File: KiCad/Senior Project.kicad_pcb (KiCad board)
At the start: 4 copper layers, 25 x 60 mm, 90 parts, among them J1 USB_C_Receptacle_USB2.0_16P, J2 Screw_Terminal_01x02, J3 Screw_Terminal_01x06, J4 Conn_ARM_JTAG_SWD_10, J5 Conn_01x02, Q2 IRLML0030, Q3 IRLML0030, Q4 IRLML0030, SW1 SW_Push, SW2 SW_Push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

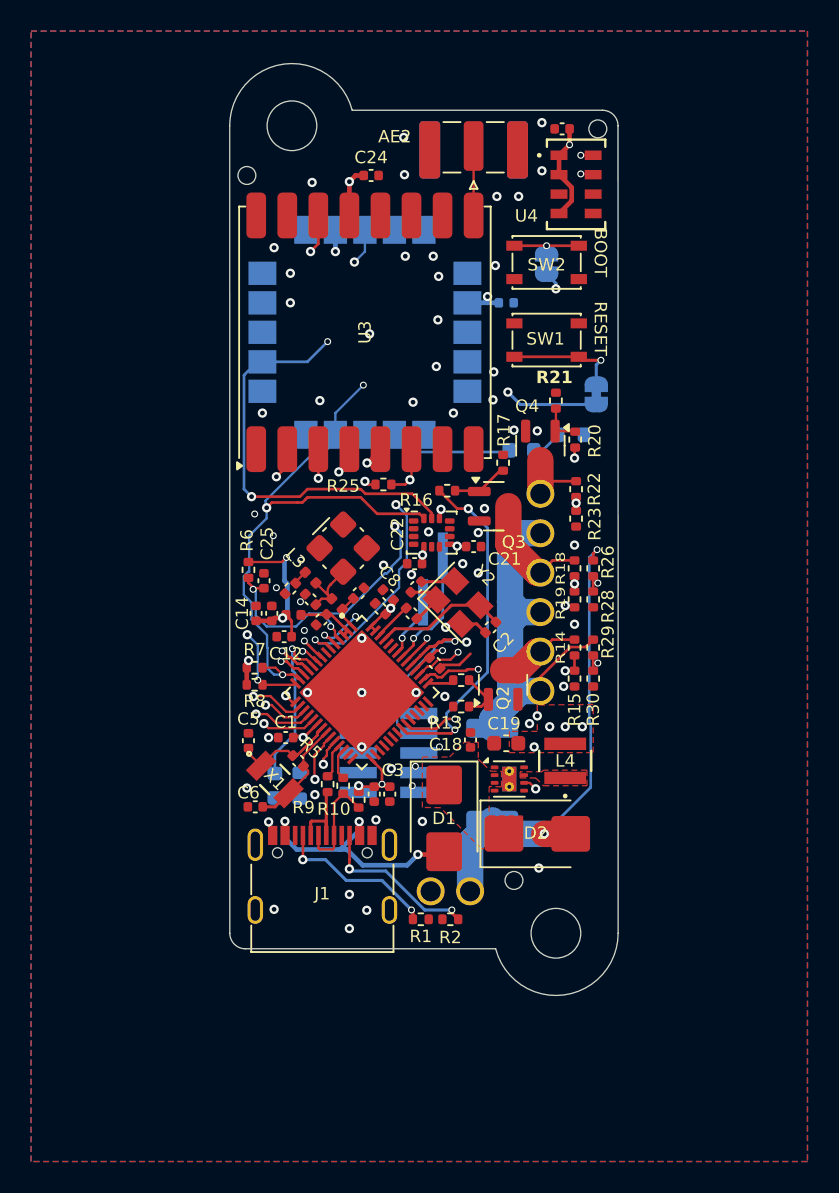
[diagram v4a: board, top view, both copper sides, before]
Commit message: switch to BMI088 for IMU
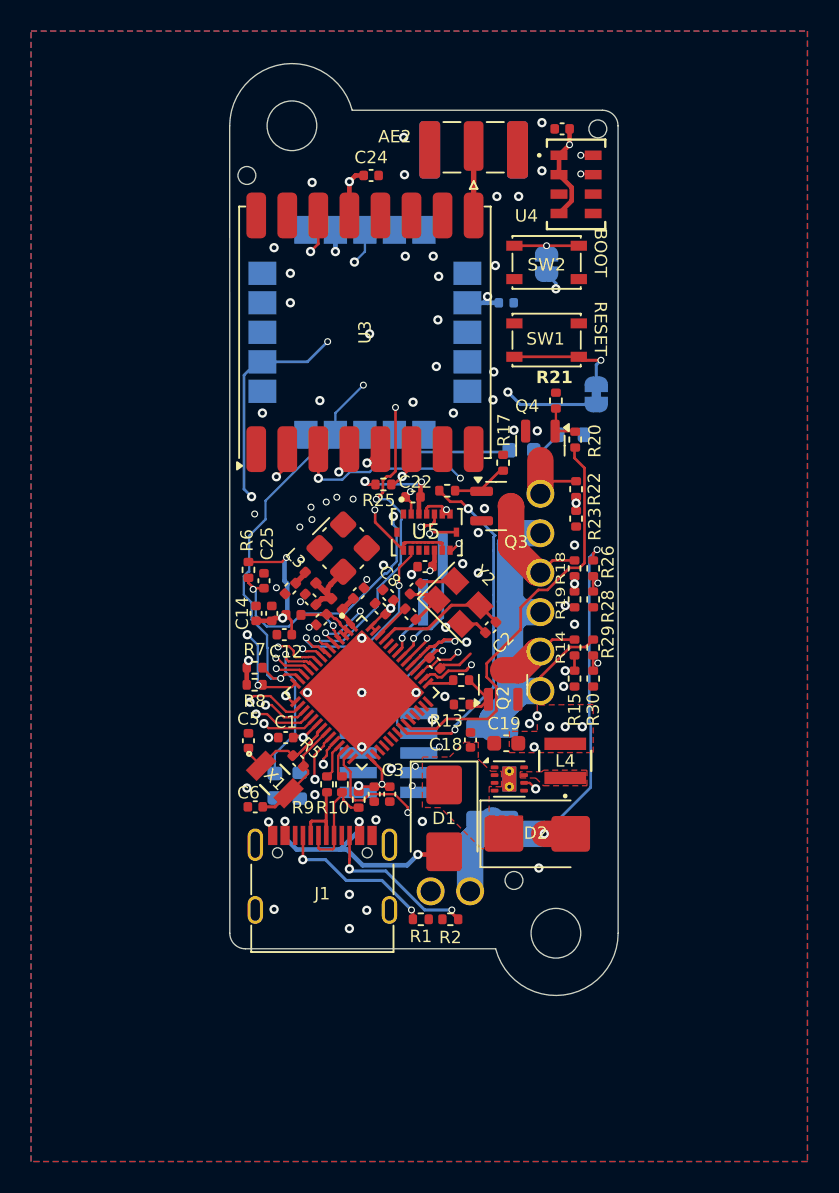
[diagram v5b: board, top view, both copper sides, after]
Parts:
- U5: value LSM6DSO32TR -> BMI088; footprint Package_LGA:LGA-14_3x2.5mm_P0.5mm_LayoutBorder3x4y -> asdt-4:PQFN50P450X300X100-16N
- moved C22 4.30 mm to (86.8, 84.9)
- moved C21 3.39 mm to (87.6, 89.4), turned to 180 degrees
- moved U5 0.32 mm to (87.7, 87.2)
- moved Q3 0.15 mm to (92.2, 85.5)
- moved R13 0.14 mm to (89.9, 98.3)
- moved C12 0.13 mm to (78.5, 93.8)
- moved C10 0.12 mm to (87.0, 90.8)
- moved R10 0.12 mm to (82.2, 103.4)
- moved R4 0.09 mm to (86.6, 92.5)
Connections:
- U1 pad 27: unconnected-(U1-GPIO21-Pad27) -> /~{GYRO_CS}
- U1 pad 7: unconnected-(U1-GPIO2-Pad7) -> /~{ACCELEROMETER_CS}
- U5 pad 1: GND -> unconnected-(U5-INT2-Pad1)
- U5 pad 10: unconnected-(U5-NC-Pad10) -> /FSPIQ
- U5 pad 11: unconnected-(U5-NC__1-Pad11) -> +3V3
- U5 pad 12: +3V3 -> unconnected-(U5-INT3-Pad12)
- U5 pad 13: /SCL -> unconnected-(U5-INT4-Pad13)
- U5 pad 14: /SDA -> /~{ACCELEROMETER_CS}
- U5 pad 3: GND -> +3V3
- U5 pad 4: unconnected-(U5-INT1-Pad4) -> GND
- U5 pad 5: +3V3 -> /~{GYRO_CS}
- U5 pad 8: +3V3 -> /FSPICLK
- U5 pad 9: unconnected-(U5-INT2-Pad9) -> /FSPID
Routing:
- net /~{GYRO_CS}: track 0.00 -> 47.1 mm, vias 0 -> 2
- net /FSPID: track 21.8 -> 41.1 mm, vias 2 -> 4
- net /FSPIQ: track 23.6 -> 41.8 mm, vias 2 -> 3
- net /~{ACCELEROMETER_CS}: track 0.00 -> 13.3 mm, vias 0 -> 2
- net /SCL: track 64.2 -> 51.7 mm
- net /SDA: track 58.0 -> 47.3 mm, vias 4 -> 3
- net /FSPICLK: track 22.3 -> 32.0 mm, vias 2 -> 3
- net /RADIO_RST: track 19.8 -> 23.9 mm
- net GND: track 6.37 -> 10.1 mm, vias 63 -> 70
- net /BATTERY_SENSE: track 26.6 -> 28.8 mm
- net /Pyro GPIO 3: track 25.8 -> 27.3 mm, vias 2 -> 0
- net +3V3: track 73.1 -> 71.7 mm, vias 21 -> 20
- net /FSPICS0: track 20.8 -> 21.9 mm
- net /GPS_Reset: track 31.1 -> 31.8 mm
- net /MTCK: track 13.8 -> 13.1 mm
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
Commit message: further refine board
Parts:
- R15, R19, R23: value 10k -> 5.1k
- moved J5 7.00 mm to (83.9, 95.8), turned to 180 degrees
- moved REF** 5.30 mm to (98.6, 109.7)
- moved C22 0.30 mm to (87.1, 84.9)
- moved Q2 0.22 mm to (92.5, 97.2)
- moved R13 0.19 mm to (89.8, 98.4)
- moved R11 0.19 mm to (91.9, 103.0)
- moved C5 0.15 mm to (76.2, 100.5)
- moved U4 0.12 mm to (97.3, 64.9)
- moved R12 0.07 mm to (89.8, 96.7)
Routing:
- net Net-(J5-Pin_1): track 7.93 -> 6.81 mm
- net /MTDI: track 12.7 -> 13.5 mm
- net +3V3: track 71.7 -> 72.3 mm
- net GND: track 10.1 -> 10.0 mm, vias 70 -> 82
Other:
- board text added: "+"
- board text added: "-"
- board text added: "A"
- board text added: "B"
- board text added: "C"
- board text added: "Max 4s"
- board text added: "PPS"
- board text added: "Status"

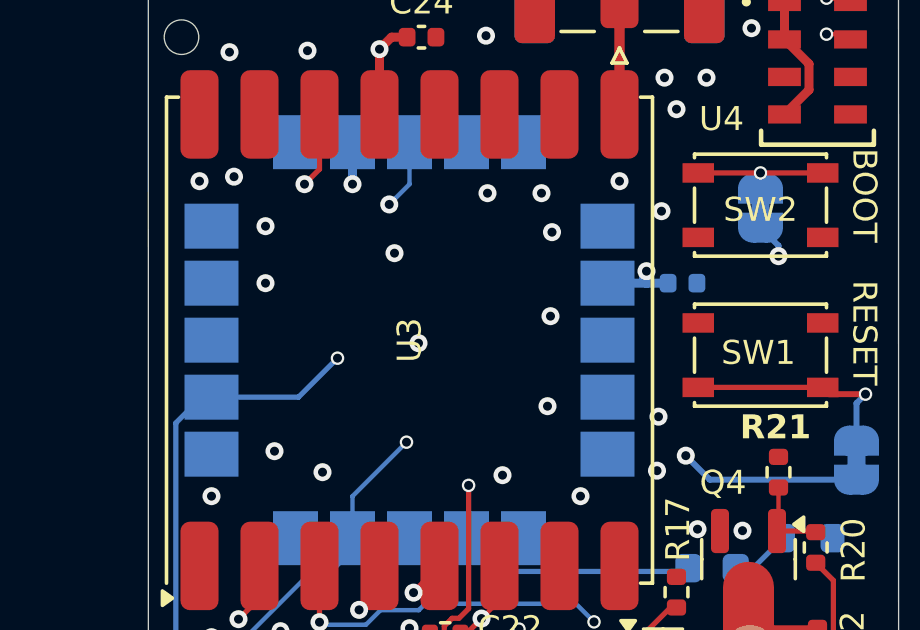
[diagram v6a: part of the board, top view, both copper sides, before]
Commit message: add OSHW logo
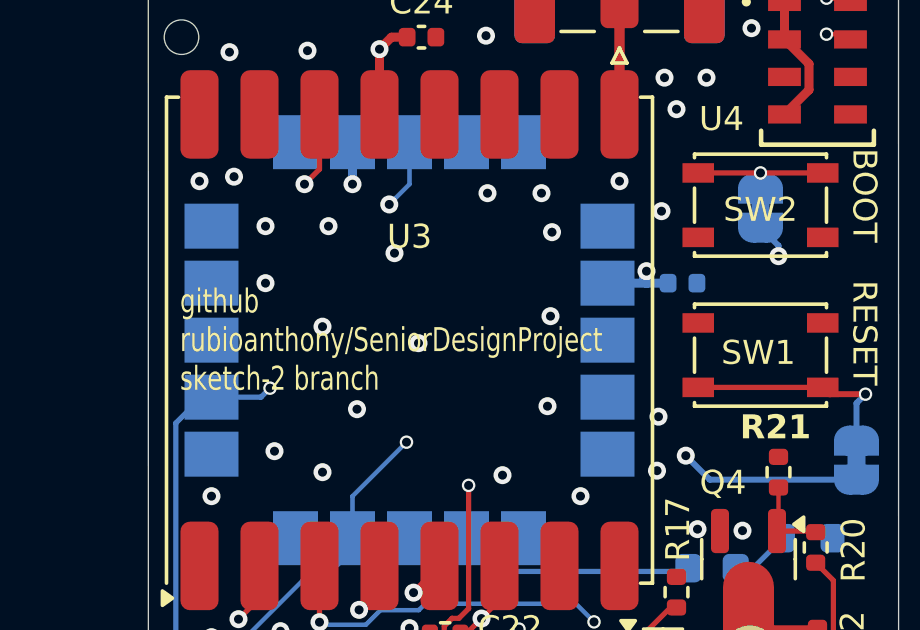
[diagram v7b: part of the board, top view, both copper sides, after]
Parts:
- added REF**: OSHW-Logo_5.7x6mm_SilkScreen, Symbol:OSHW-Logo_5.7x6mm_SilkScreen, B.Cu at (96.8, 105.5)
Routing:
- net /Interrupt: track 36.9 -> 40.3 mm
- net +3V3: track 72.3 -> 69.8 mm
- net GND: vias 82 -> 85
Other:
- board text added: "2025-04-07"
- board text added: "github rubioanthony/SeniorDesignProject sketch-2 branch"
- board text removed: "2025-04-06"
